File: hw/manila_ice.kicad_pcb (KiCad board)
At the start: 4 copper layers, 85 x 54 mm, 146 parts, among them J1 USB_B, J2 RB1-125B8G1A, J3 Conn_01x08, J4 Conn_02x06_Odd_Even, J5 Conn_02x06_Odd_Even, SW1 SW_SPST, SW2 SW_SPST, SW3 SW_SPST, U1 W9812G6KH-6, U2 CH340E, U3 TPS54331D, U4 TPS54331D, U5 RTL8211EG-VB-CG, U6 ICE40HX4K-TQ144, U7 W25Q128JVS, U8 M24C01-RMN, X1 SG-7050CAN, X2 SG-7050CAN

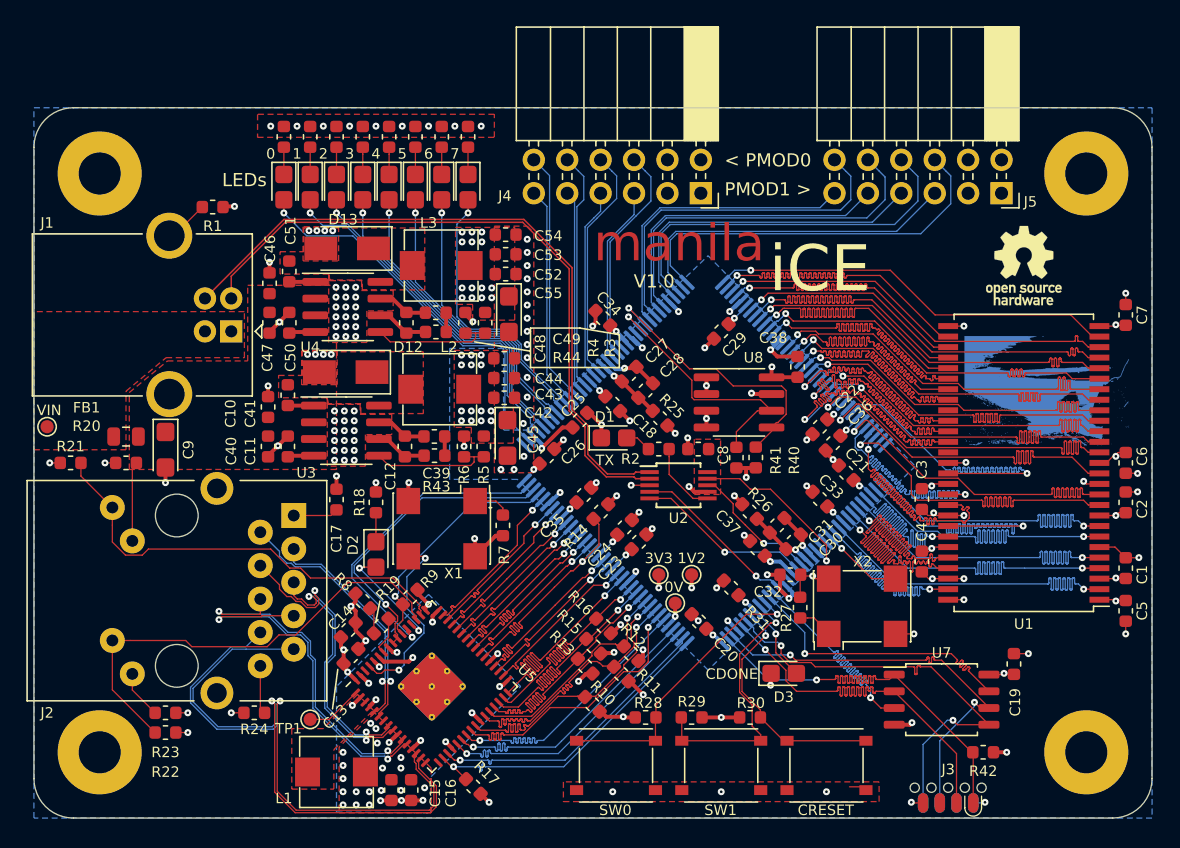
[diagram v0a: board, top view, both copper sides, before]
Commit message: Fixed tant footprint. Added JLC part numbers to other components
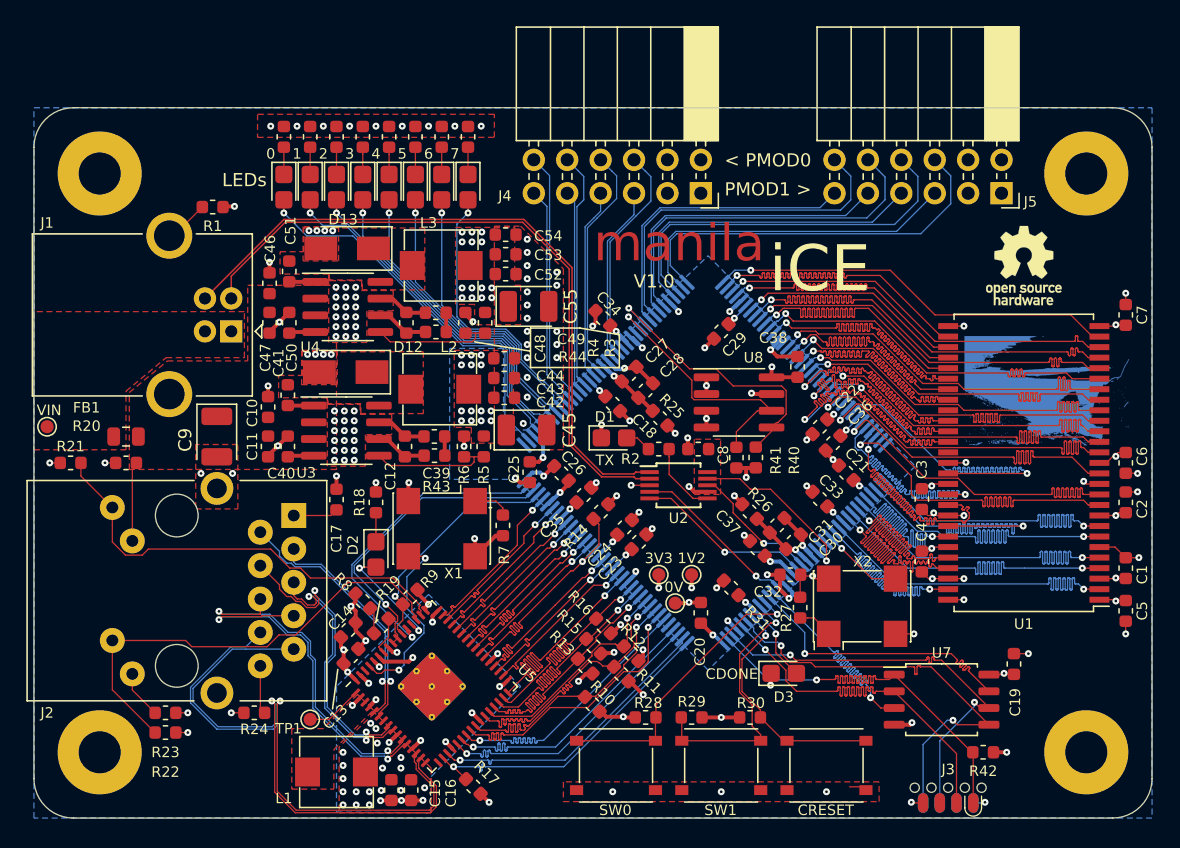
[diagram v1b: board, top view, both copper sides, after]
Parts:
- C12, C48: value C -> 10p
- C39, C49: value C -> 1n
- C45, C55, C9: footprint Capacitor_Tantalum_SMD:CP_EIA-3216-18_Kemet-A -> Capacitor_Tantalum_SMD:CP_EIA-3528-21_Kemet-B
- R43, R44: value R -> 43k
- moved C25 5.49 mm to (151.5, 97.7), turned to 270 degrees
- moved C9 4.03 mm to (127.7, 95.0)
- moved C26 1.70 mm to (153.9, 97.8), turned to 315 degrees
- moved C55 1.60 mm to (151.4, 85.1), turned to 0 degrees
- moved C45 1.57 mm to (151.2, 94.5), turned to 0 degrees
- moved C20 0.67 mm to (164.5, 108.4), turned to 90 degrees
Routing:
- net +3V3: track 75.2 -> 77.4 mm
- net +1V2: track 12.3 -> 11.2 mm
- net GND: track 100.3 -> 99.4 mm, vias 145 -> 147
